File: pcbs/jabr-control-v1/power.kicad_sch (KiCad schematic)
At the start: 0 parts

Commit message: Added PCIe connections
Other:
- added sheet Power In (power-in.kicad_sch)
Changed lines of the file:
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@@
 	(generator_version "9.0")
 	(paper "A4")
+	(sheet
+		(at 76.2 76.2)
+		(size 25.4 25.4)
+		(exclude_from_sim no)
+		(in_bom yes)
+		(on_board yes)
+		(dnp no)
+		(fields_autoplaced yes)
+		(stroke
+			(width 0.1524)
+			(type solid)
+		)
+		(fill
+			(color 0 0 0 0.0000)
+		)
+		(property "Sheetname" "Power In"
+			(at 76.2 75.4884 0)
+			(effects
+				(font
+					(size 1.27 1.27)
+				)
+				(justify left bottom)
+			)
+		)
+		(property "Sheetfile" "power-in.kicad_sch"
+			(at 76.2 102.1846 0)
+			(effects
+				(font
+					(size 1.27 1.27)
+				)
+				(justify left top)
+			)
+		)
+		(instances
+			(project "jabr-control-v1"
+				(path "/f91ec272-d09a-4038-bbbb-962739a92c51/3f551047-3bb0-4f63-99e0-34fd9061d844"
+					(page "12")
+				)
+			)
+		)
+	)
 )

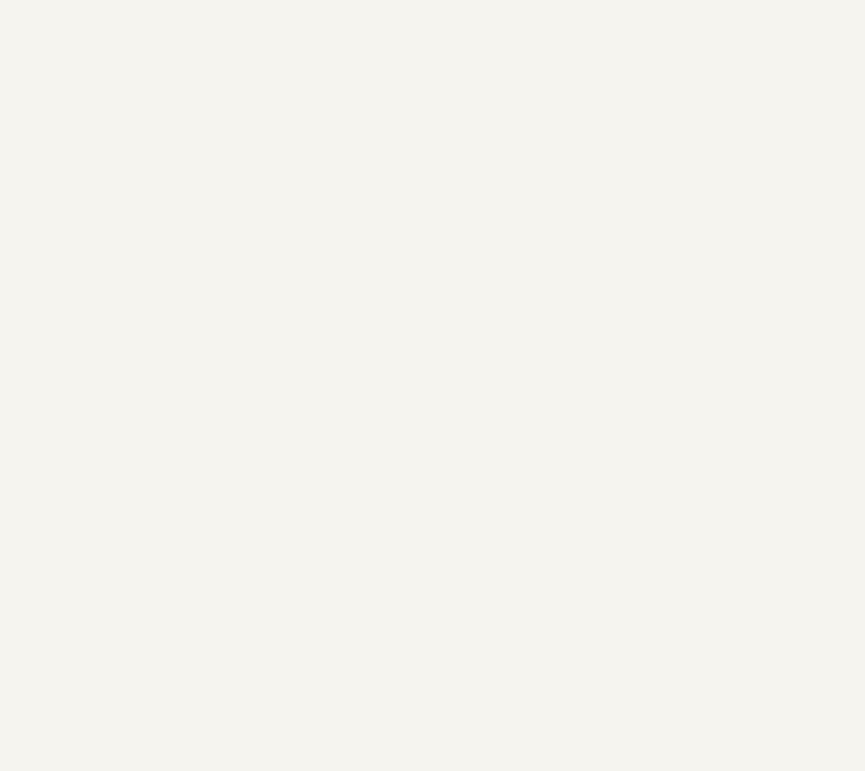
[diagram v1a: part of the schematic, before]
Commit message: Added power sheets
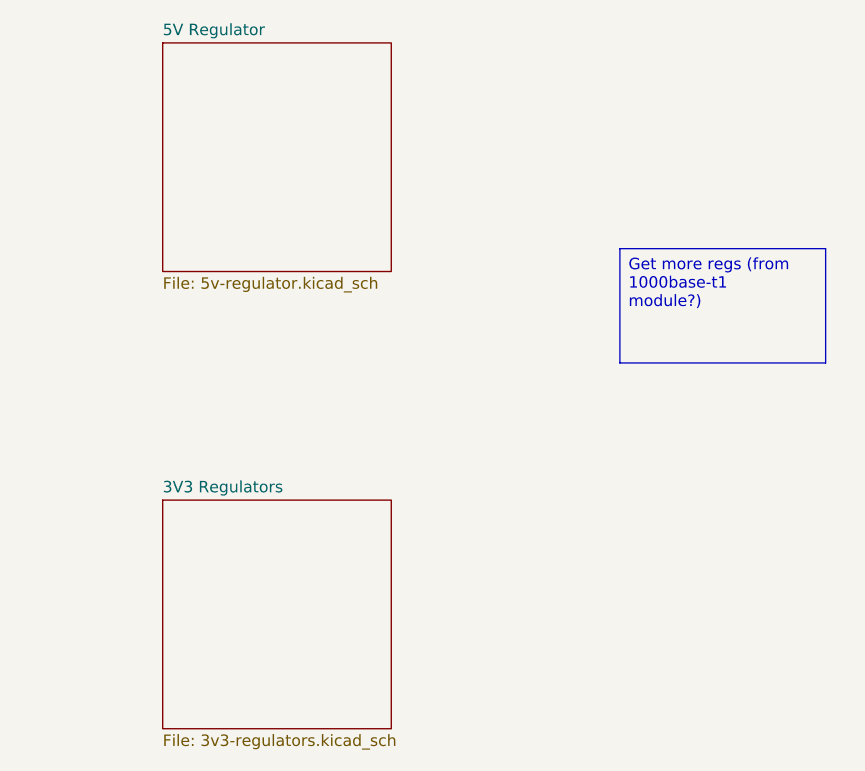
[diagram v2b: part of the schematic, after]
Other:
- added sheet 3V3 Regulators (3v3-regulators.kicad_sch)
- added sheet 5V Regulator (5v-regulator.kicad_sch)
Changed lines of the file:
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@@
 	(generator_version "9.0")
 	(paper "A4")
+	(text_box "Get more regs (from 1000base-t1 module?)"
+		(exclude_from_sim no)
+		(at 177.8 99.06 0)
+		(size 22.86 12.7)
+		(margins 0.9525 0.9525 0.9525 0.9525)
+		(stroke
+			(width 0)
+			(type solid)
+			(color 255 0 0 1)
+		)
+		(fill
+			(type none)
+		)
+		(effects
+			(font
+				(size 1.27 1.27)
+				(color 255 0 0 1)
+			)
+			(justify left top)
+		)
+	)
+	(sheet
+		(at 127 127)
+		(size 25.4 25.4)
+		(exclude_from_sim no)
+		(in_bom yes)
+		(on_board yes)
+		(dnp no)
+		(fields_autoplaced yes)
+		(stroke
+			(width 0.1524)
+			(type solid)
+		)
+		(fill
+			(color 0 0 0 0.0000)
+		)
+		(property "Sheetname" "3V3 Regulators"
+			(at 127 126.2884 0)
+			(effects
+				(font
+					(size 1.27 1.27)
+				)
+				(justify left bottom)
+			)
+		)
+		(property "Sheetfile" "3v3-regulators.kicad_sch"
+			(at 127 152.9846 0)
+			(effects
+				(font
+					(size 1.27 1.27)
+				)
+				(justify left top)
+			)
+		)
+		(instances
+			(project "jabr-control-v1"
+				(path "/f91ec272-d09a-4038-bbbb-962739a92c51/3f551047-3bb0-4f63-99e0-34fd9061d844"
+					(page "14")
+				)
+			)
+		)
+	)
+	(sheet
+		(at 127 76.2)
+		(size 25.4 25.4)
+		(exclude_from_sim no)
+		(in_bom yes)
+		(on_board yes)
+		(dnp no)
+		(fields_autoplaced yes)
+		(stroke
+			(width 0.1524)
+			(type solid)
+		)
+		(fill
+			(color 0 0 0 0.0000)
+		)
+		(property "Sheetname" "5V Regulator"
+			(at 127 75.4884 0)
+			(effects
+				(font
+					(size 1.27 1.27)
+				)
+				(justify left bottom)
+			)
+		)
+		(property "Sheetfile" "5v-regulator.kicad_sch"
+			(at 127 102.1846 0)
+			(effects
+				(font
+					(size 1.27 1.27)
+				)
+				(justify left top)
+			)
+		)
+		(instances
+			(project "jabr-control-v1"
+				(path "/f91ec272-d09a-4038-bbbb-962739a92c51/3f551047-3bb0-4f63-99e0-34fd9061d844"
+					(page "13")
+				)
+			)
+		)
+	)
 	(sheet
 		(at 76.2 76.2)

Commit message: Worked on power and other areas of the schematic
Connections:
- no-connect marks 0 -> 1
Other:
- added sheet 1V1 Regulator (1v2-regulator.kicad_sch)
- sheet 3V3 Regulators ports: added 3V3_M2_EN, 3V3_M2_MODE; removed none
- sheet 5V Regulator ports: added INH; removed none
- note added: "1000BASE-T1"
- note added: "1V1"
- note added: "1V8"
- note added: "23mA"
- note added: "3V3"
- note added: "3V3_AON"
- note added: "3V3_M2"
- note added: "480mA"
- note added: "6uA"
- note added: "90mA"
- note added: "<3000mA"
- note added: "<300mA"
- note added: "<500mA"
- note added: "<5mA"
- note added: "CM5"
- note added: "CM5 VBAT"
- note added: "CM5IO"
- note added: "LAN7431"
- note added: "M.2 E-Key connector"
- note added: "M.2 SUSCLK"
- note added: "PCIe Switch (1.0V to 1.3V)"
- note added: "PHY Wakeup circuitry"
- note added: "VBUS"

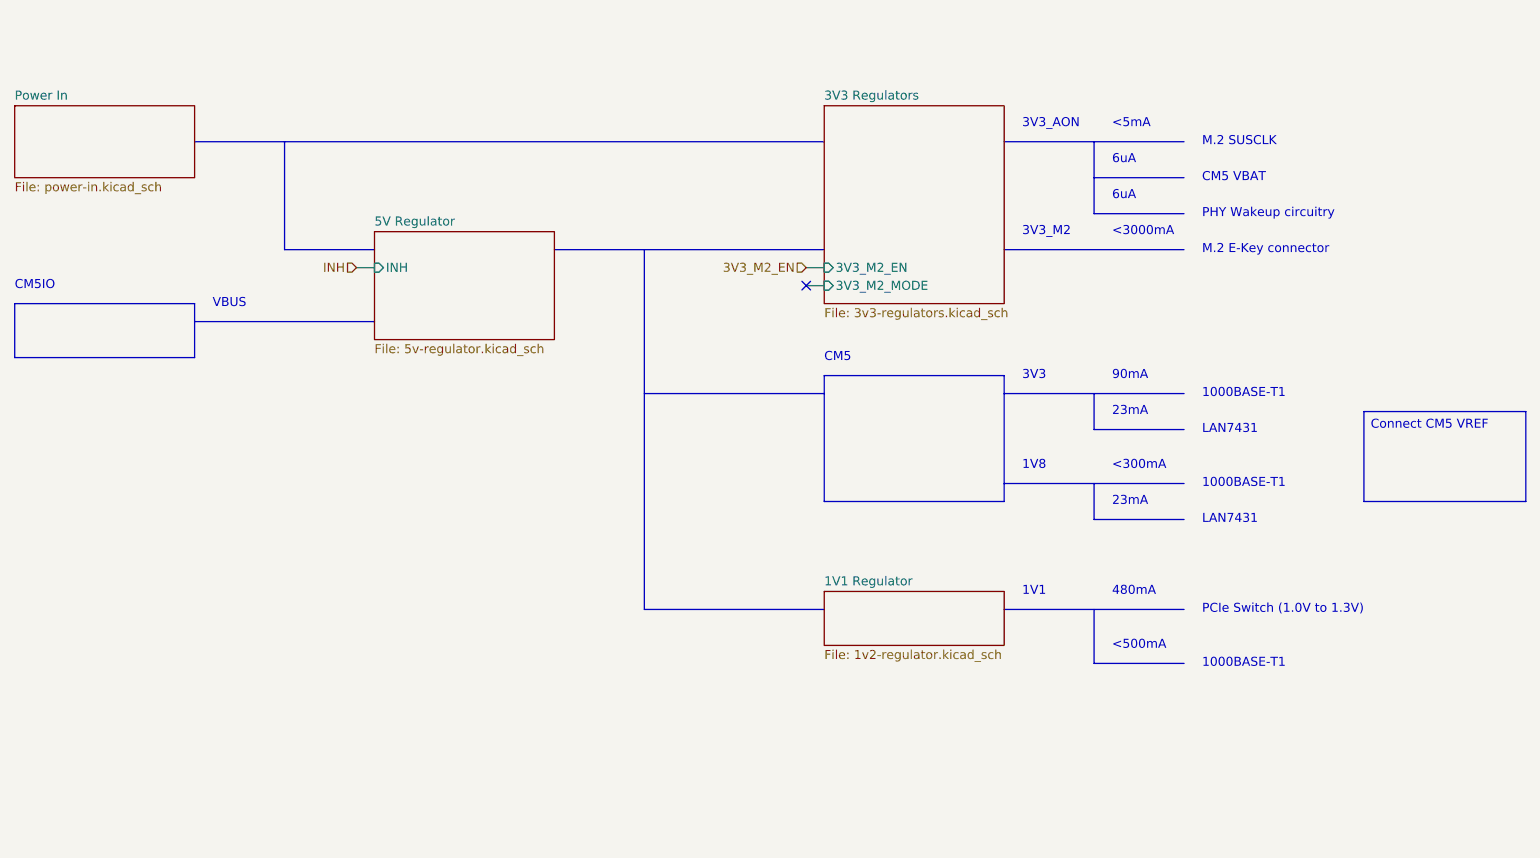
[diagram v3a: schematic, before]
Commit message: Consolodated 1V1 and 1V0 regulators into one sheet
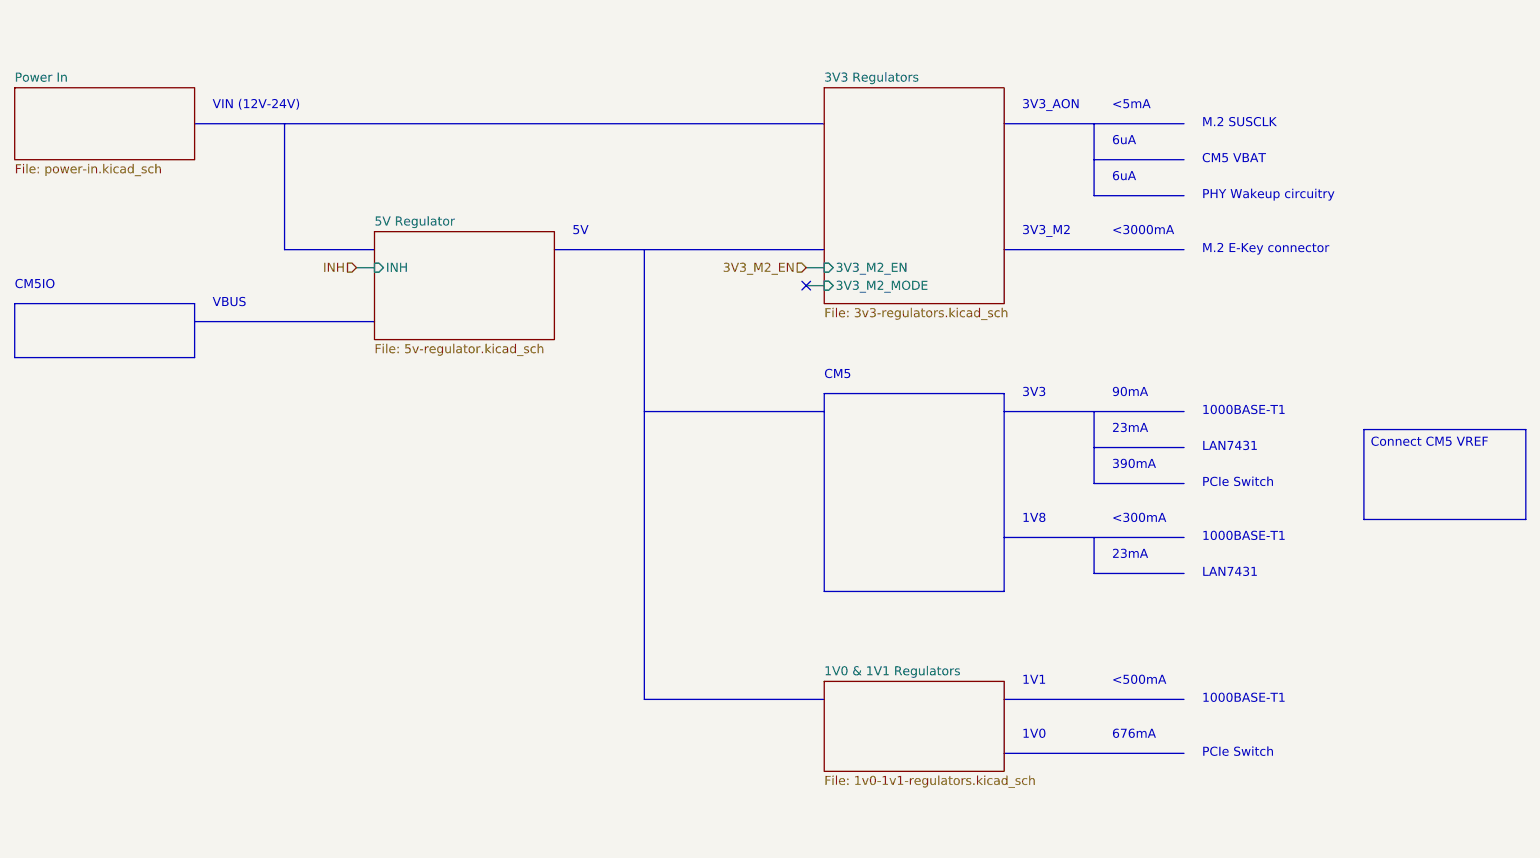
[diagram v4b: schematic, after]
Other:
- sheet 1V1 Regulator renamed 1V0 & 1V1 Regulators
- sheet 1V0 & 1V1 Regulators: file 1v2-regulator.kicad_sch -> 1v0-1v1-regulators.kicad_sch
- note added: "1V0"
- note added: "390mA"
- note added: "5V"
- note added: "676mA"
- note added: "PCIe Switch"
- note added: "VIN (12V-24V)"
- note removed: "480mA"
- note removed: "PCIe Switch (1.0V to 1.3V)"

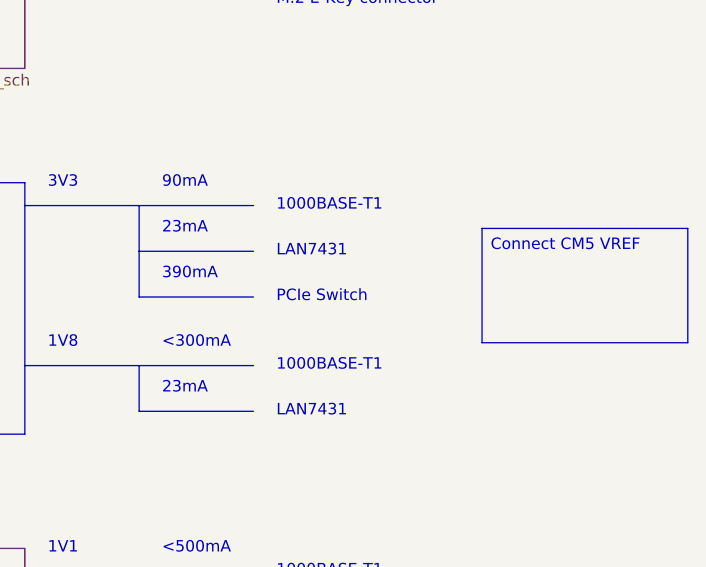
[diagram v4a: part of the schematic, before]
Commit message: Progress on LAN7431 power
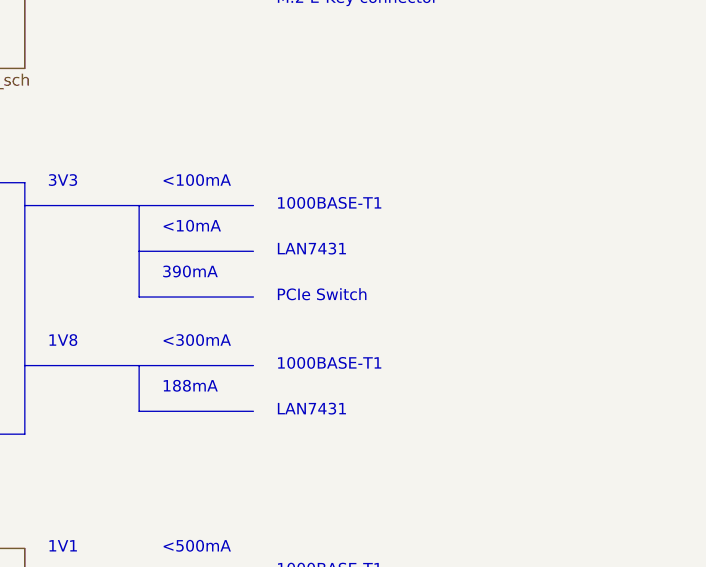
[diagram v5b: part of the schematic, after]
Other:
- note added: "188mA"
- note added: "<100mA"
- note added: "<10mA"
- note removed: "23mA"
- note removed: "90mA"

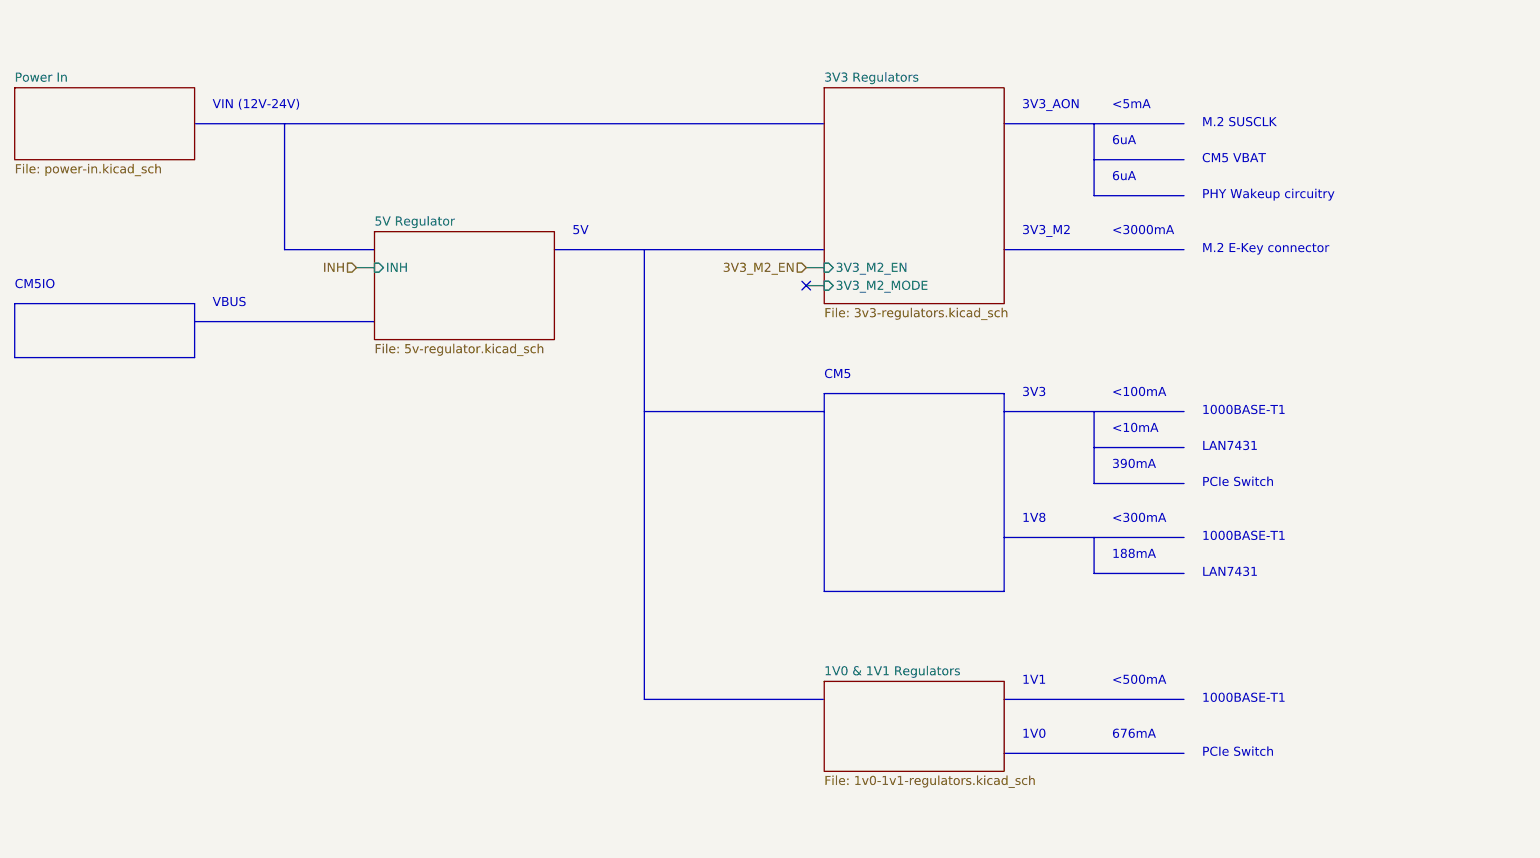
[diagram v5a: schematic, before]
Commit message: Schematic nearing completion, need to do GPIO and PHY decouplings caps
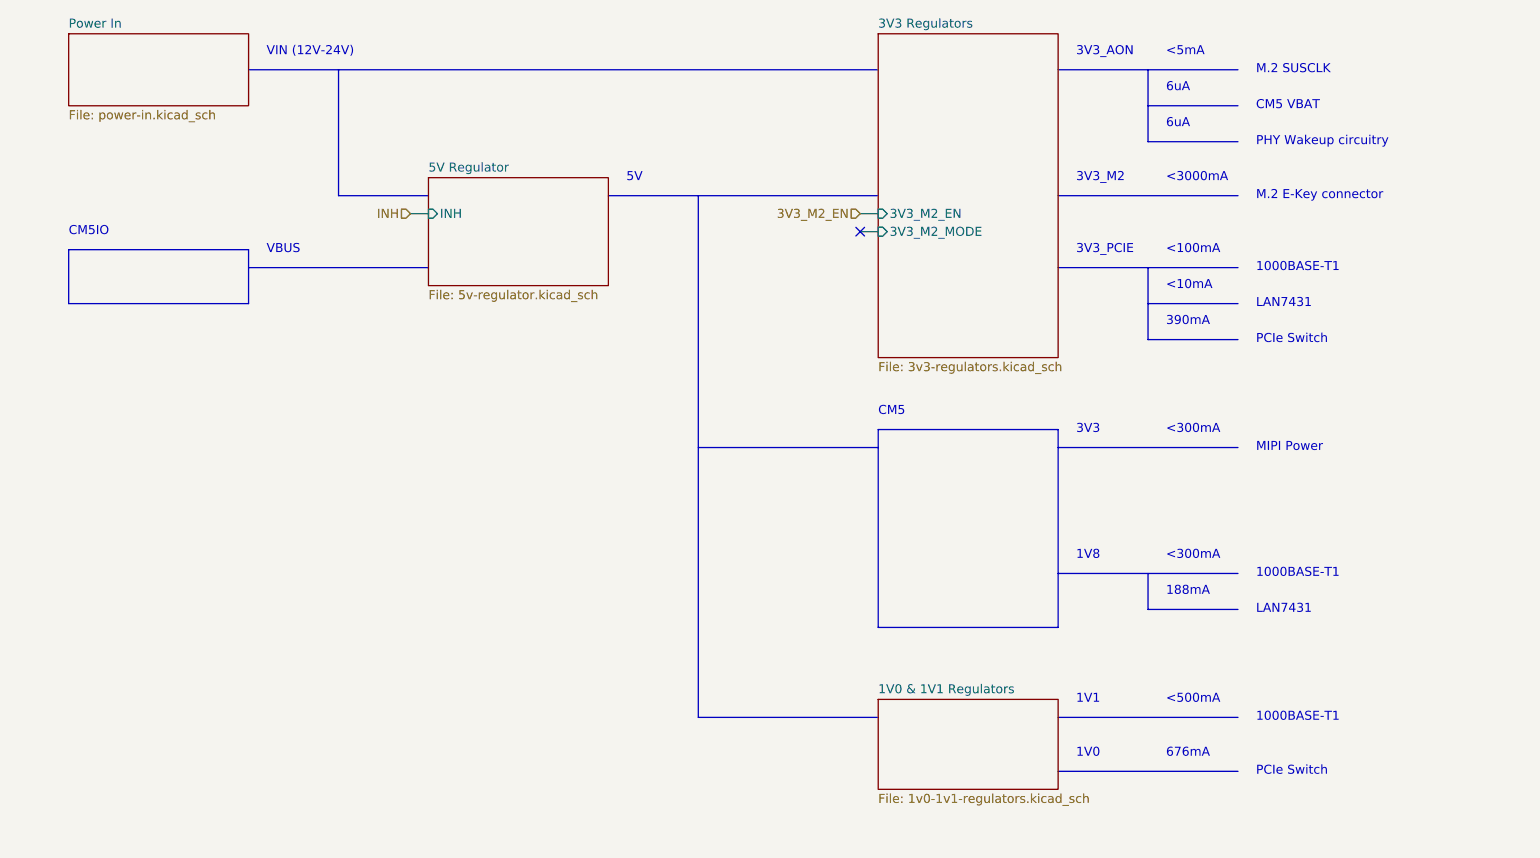
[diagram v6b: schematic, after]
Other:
- note added: "3V3_PCIE"
- note added: "MIPI Power"
